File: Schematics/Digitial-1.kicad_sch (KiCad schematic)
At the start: 13 parts, among them J18 Conn_01x02, J19 To Compute #1, J20 Conn_01x04, J21 Conn_01x04, J22 Conn_01x02, J23 To Compute #1, U16 LM1117-5.0, U17 ESP32-DEVKIT-V1, U18 USB Host Shield 2.0

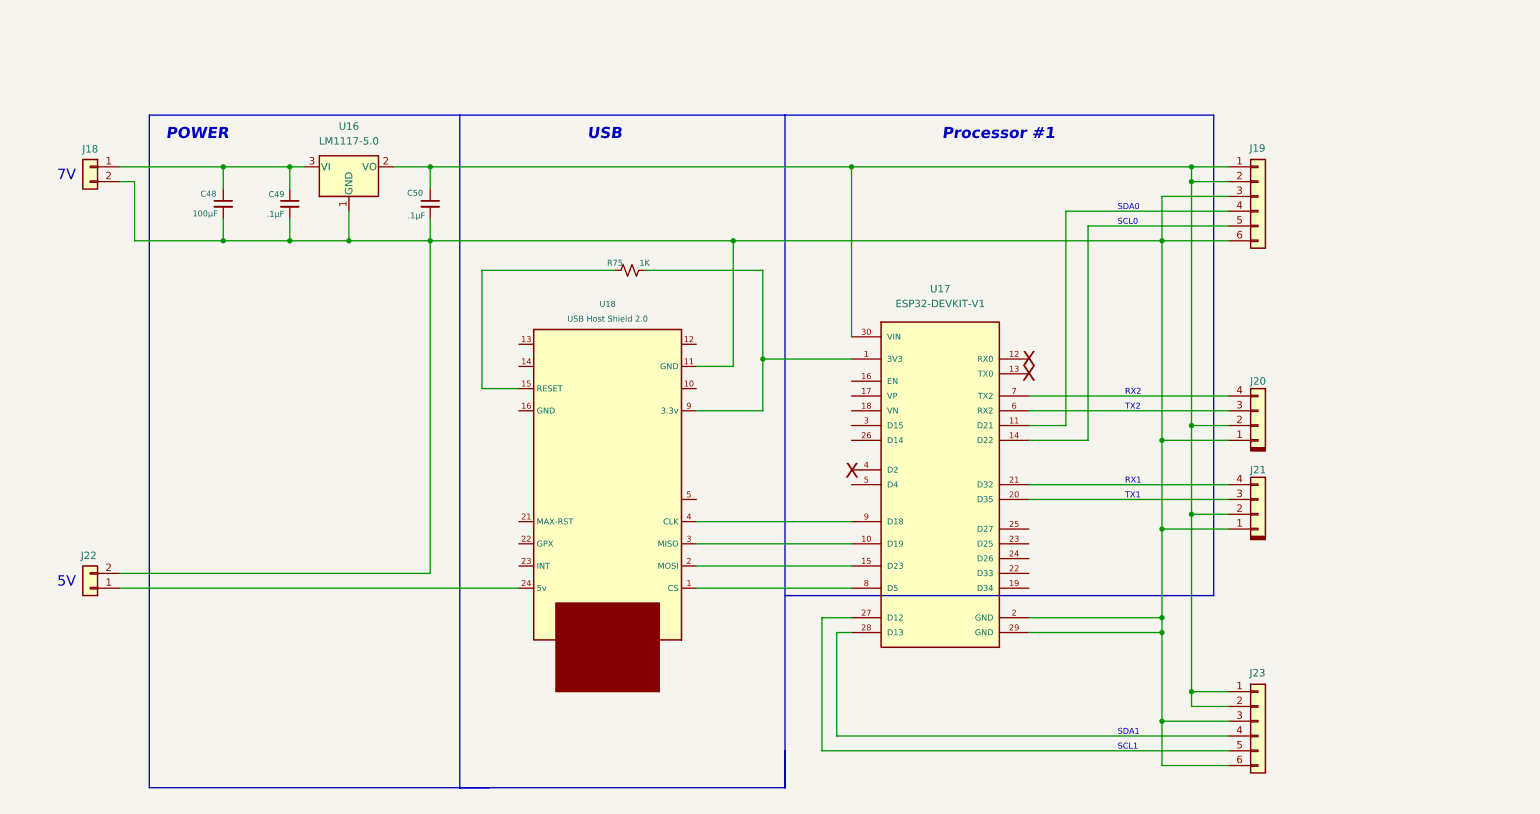
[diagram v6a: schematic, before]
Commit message: working interface for 7 inch display with occasional faults.
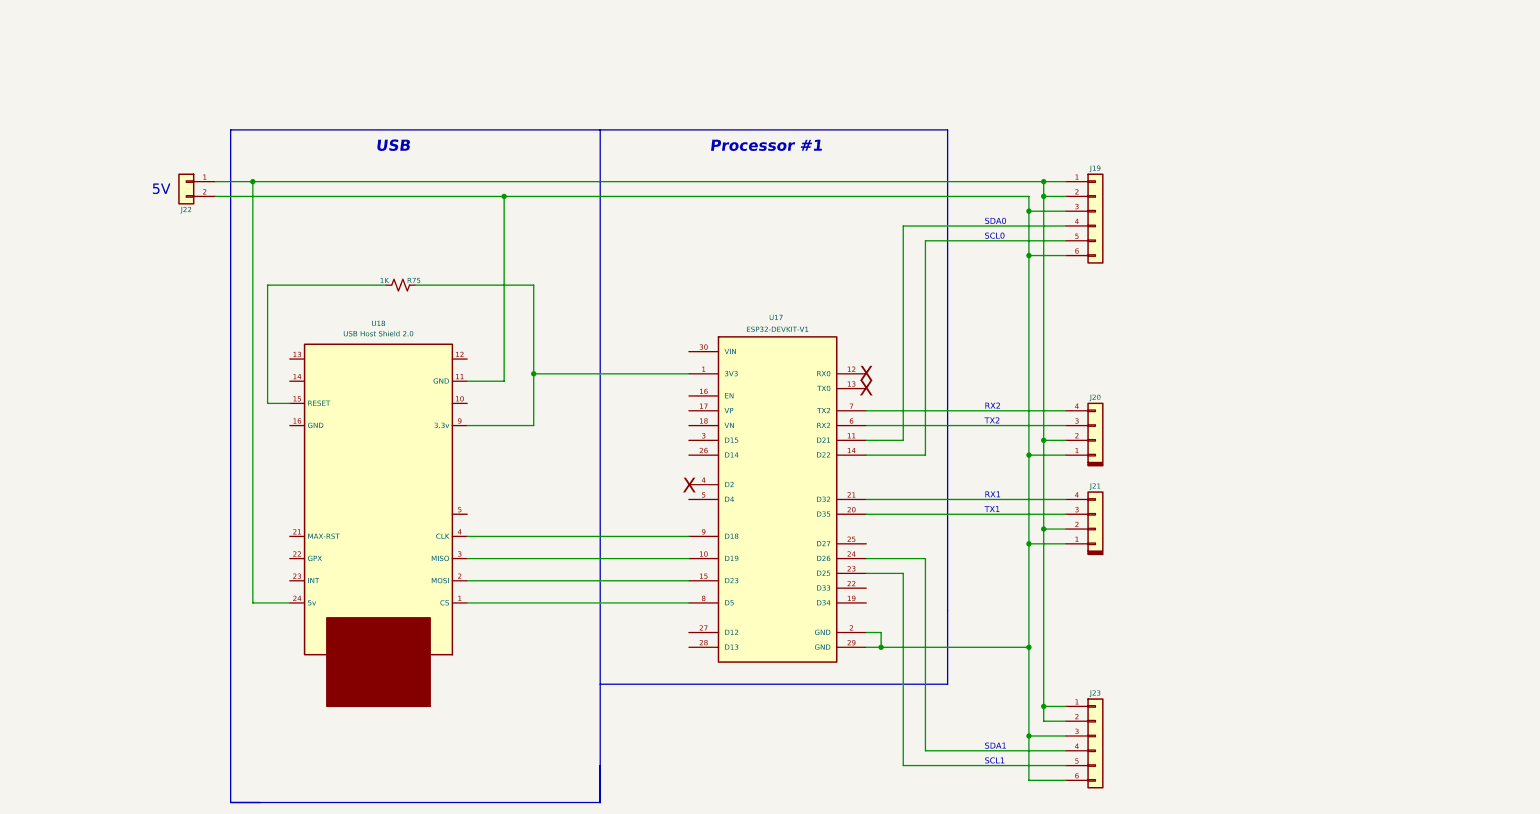
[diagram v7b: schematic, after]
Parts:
- removed C48: 100µF, symbol Device:C_Small
- removed C49, C50: .1µF, symbol Device:C_Small
- removed J18: Conn_01x02, symbol Connector_Generic:Conn_01x02
- removed U16: LM1117-5.0, symbol Regulator_Linear:LM1117-5.0
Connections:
- net at U17.23 (D25): now also J23.5 (Pin_5)
- net at U17.24 (D26): now also J23.4 (Pin_4)
- net at U17.27 (D12): no longer J23.5 (Pin_5)
- net at U17.28 (D13): no longer J23.4 (Pin_4)
- net at J19.1 (Pin_1), J19.2 (Pin_2), J20.2 (Pin_2)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: now also J22.1 (Pin_1), U18.24 (5v); no longer U17.30 (VIN)
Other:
- note removed: "7V"
- note removed: "POWER"
- moved on the sheet: J19, J21, J22, J23, R75, U17, U18

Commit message: Reset handshake completed.
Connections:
- net at U17.25 (D27): now also J23.2 (Pin_2)
- net at J19.1 (Pin_1), J19.2 (Pin_2), J20.2 (Pin_2)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: no longer J23.2 (Pin_2)
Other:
- note added: "Startup Strobe"
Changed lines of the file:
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@@
-	)
-	(junction
-		(at 234.95 135.89)
-		(diameter 0)
-		(color 0 0 0 0)
 	)
 	(junction
@@
 	(wire
 		(pts
+			(xy 204.47 107.95) (xy 218.44 107.95)
+		)
+		(stroke
+			(width 0)
+			(type default)
+		)
+	)
+	(wire
+		(pts
 			(xy 238.76 105.41) (xy 234.95 105.41)
 		)
@@
 	(polyline
 		(pts
-			(xy 158.75 132.08) (xy 218.44 132.08)
+			(xy 158.75 132.08) (xy 223.52 132.08)
+		)
+		(stroke
+			(width 0)
+			(type default)
+		)
+	)
+	(wire
+		(pts
+			(xy 218.44 107.95) (xy 218.44 138.43)
 		)
 		(stroke
@@
 	(polyline
 		(pts
-			(xy 218.44 119.38) (xy 218.44 132.08)
+			(xy 223.52 119.38) (xy 223.52 132.08)
 		)
 		(stroke
@@
 	(wire
 		(pts
+			(xy 218.44 138.43) (xy 238.76 138.43)
+		)
+		(stroke
+			(width 0)
+			(type default)
+		)
+	)
+	(wire
+		(pts
 			(xy 238.76 45.72) (xy 234.95 45.72)
 		)
@@
 	(wire
 		(pts
-			(xy 234.95 138.43) (xy 238.76 138.43)
-		)
-		(stroke
-			(width 0)
-			(type default)
-		)
-	)
-	(wire
-		(pts
 			(xy 210.82 113.03) (xy 210.82 146.05)
 		)
@@
 	(polyline
 		(pts
-			(xy 158.75 36.83) (xy 218.44 36.83)
-		)
-		(stroke
-			(width 0)
-			(type default)
-		)
-	)
-	(wire
-		(pts
-			(xy 234.95 135.89) (xy 234.95 138.43)
+			(xy 158.75 36.83) (xy 223.52 36.83)
 		)
 		(stroke
@@
 	(polyline
 		(pts
-			(xy 218.44 36.83) (xy 218.44 119.38)
+			(xy 223.52 36.83) (xy 223.52 119.38)
 		)
 		(stroke
@@
 		(effects
 			(font
+				(size 1.016 1.016)
+			)
+			(justify left bottom)
+		)
+	)
+	(text "Startup Strobe"
+		(exclude_from_sim no)
+		(at 219.202 138.43 0)
+		(effects
+			(font
